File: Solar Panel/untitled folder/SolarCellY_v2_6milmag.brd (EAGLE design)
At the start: 100 x 82 mm, 23 parts

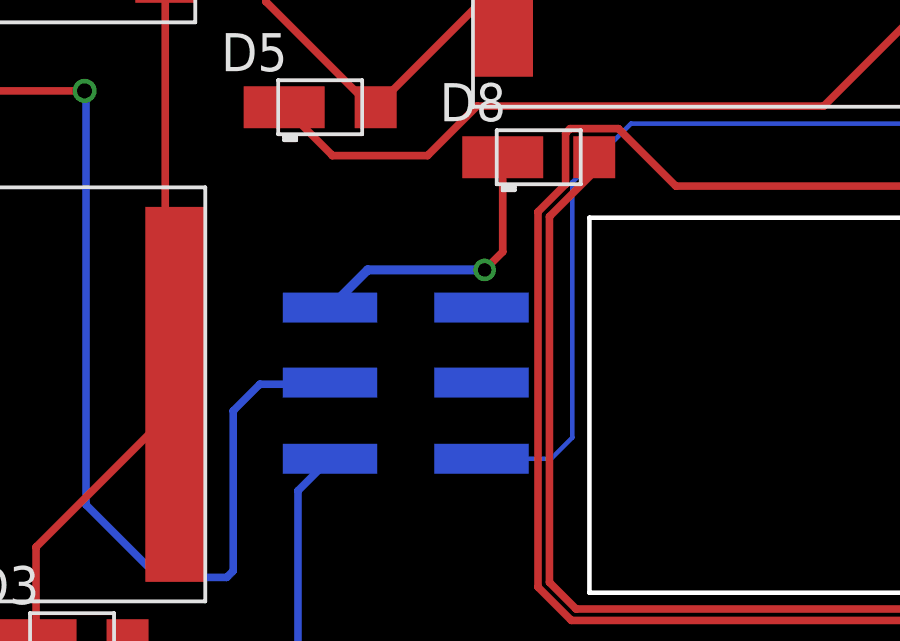
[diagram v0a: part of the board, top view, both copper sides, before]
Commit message: Finalized Y and created gerbers
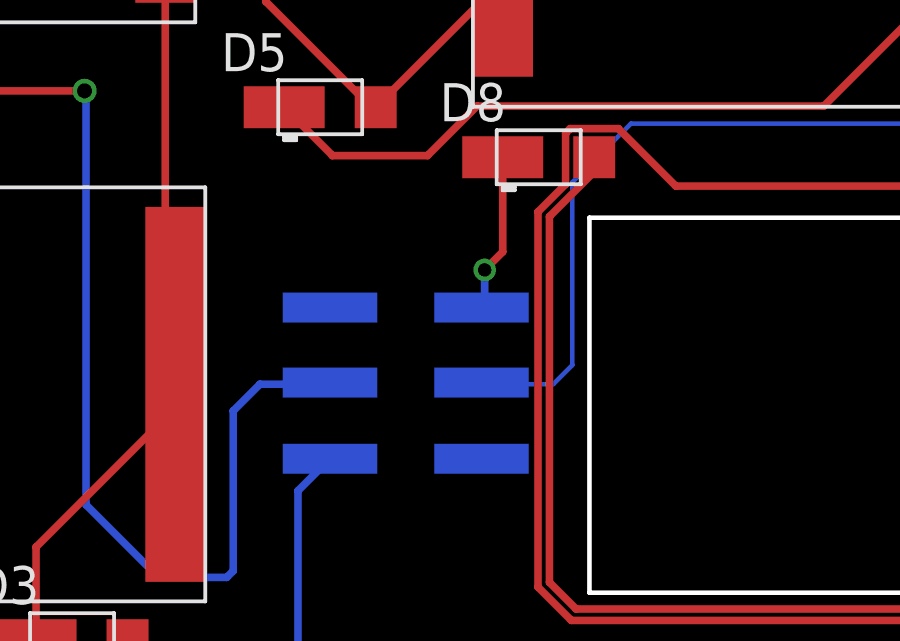
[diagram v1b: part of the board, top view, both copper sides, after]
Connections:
- net N$1: now also U$1.P$4; no longer U$1.P$2
- net N$14: now also U$1.P$6; no longer U$1.P$5
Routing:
- net N$14: track 9.68 -> 5.40 mm
- net N$1: track 54673.9 -> 54671.7 mm
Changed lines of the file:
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@@
 <layers>
 <layer number="1" name="Top" color="4" fill="1" visible="yes" active="yes"/>
-<layer number="2" name="Route2" color="16" fill="1" visible="yes" active="yes"/>
+<layer number="2" name="Route2" color="16" fill="1" visible="no" active="yes"/>
 <layer number="3" name="Route3" color="17" fill="1" visible="no" active="no"/>
 <layer number="4" name="Route4" color="18" fill="1" visible="no" active="no"/>
@@
 <wire x1="72.8472" y1="59.2836" x2="72.8472" y2="22.5552" width="0.1524" layer="15"/>
 <wire x1="72.8472" y1="22.5552" x2="27.7368" y2="22.5552" width="0.1524" layer="15"/>
+<contactref element="U$1" pad="P$4"/>
 <contactref element="U$1" pad="P$3"/>
 <wire x1="41.148" y1="50.546" x2="41.195115625" y2="50.546" width="0.254" layer="16"/>
@@
 <wire x1="41.148" y1="50.546" x2="9.906" y2="50.546" width="0.254" layer="1"/>
 <wire x1="9.906" y1="50.546" x2="8.636" y2="51.816" width="0.254" layer="1"/>
+<wire x1="72.5424" y1="48.895" x2="68.58" y2="48.895" width="0.1524" layer="2"/>
 <wire x1="8.636" y1="51.816" x2="2.413" y2="51.816" width="0.254" layer="1"/>
 <wire x1="2.413" y1="51.816" x2="2.286" y2="51.943" width="0.254" layer="1"/>
@@
 <wire x1="72.5424" y1="49.4538" x2="59.3598" y2="49.4538" width="0.1524" layer="16"/>
 <wire x1="59.3598" y1="49.4538" x2="57.404" y2="47.498" width="0.1524" layer="16"/>
-<wire x1="57.404" y1="47.498" x2="57.404" y2="38.989" width="0.1524" layer="16"/>
+<wire x1="56.769" y1="40.767" x2="54.356" y2="40.767" width="0.1524" layer="16"/>
+<wire x1="57.404" y1="47.498" x2="57.404" y2="41.402" width="0.1524" layer="16"/>
+<wire x1="57.404" y1="41.402" x2="56.769" y2="40.767" width="0.1524" layer="16"/>
 <wire x1="72.8472" y1="59.2836" x2="27.432" y2="59.2836" width="0.1524" layer="16"/>
+<wire x1="68.58" y1="48.895" x2="68.707" y2="48.768" width="0.1524" layer="2"/>
 <wire x1="68.707" y1="48.768" x2="68.707" y2="48.26" width="0.1524" layer="2"/>
+<wire x1="54.356" y1="40.767" x2="54.377" y2="40.822" width="0" layer="19" extent="16-16"/>
+<wire x1="27.432" y1="59.2836" x2="27.432" y2="59.2836" width="0" layer="19" extent="2-15"/>
+<wire x1="49.327" y1="40.822" x2="49.657" y2="40.767" width="0" layer="19" extent="16-16"/>
 <via x="68.707" y="48.26" extent="1-16" drill="0.45"/>
-<contactref element="U$1" pad="P$2"/>
-<wire x1="57.404" y1="38.989" x2="56.697" y2="38.282" width="0.1524" layer="16"/>
-<wire x1="56.697" y1="38.282" x2="54.377" y2="38.282" width="0.1524" layer="16"/>
-<wire x1="72.5424" y1="48.895" x2="68.834" y2="48.895" width="0.1524" layer="2"/>
-<wire x1="68.834" y1="48.895" x2="68.707" y2="48.768" width="0.1524" layer="2"/>
-<wire x1="49.657" y1="40.767" x2="49.327" y2="40.822" width="0" layer="19" extent="16-16"/>
-<wire x1="72.8472" y1="59.2836" x2="72.8472" y2="59.2836" width="0" layer="19" extent="2-15"/>
 </signal>
 <signal name="N$4">
@@
 <signal name="N$14">
 <contactref element="D8" pad="NEG"/>
+<contactref element="U$1" pad="P$6"/>
 <wire x1="55.085" y1="48.333" x2="55.085" y2="45.179" width="0.254" layer="1"/>
 <wire x1="55.085" y1="45.179" x2="54.483" y2="44.577" width="0.254" layer="1"/>
 <via x="54.483" y="44.577" extent="1-16" drill="0.45"/>
-<contactref element="U$1" pad="P$5"/>
-<wire x1="54.483" y1="44.577" x2="50.582" y2="44.577" width="0.3048" layer="16"/>
-<wire x1="50.582" y1="44.577" x2="49.327" y2="43.322" width="0.3048" layer="16"/>
+<wire x1="54.483" y1="44.577" x2="54.483" y2="43.18" width="0.254" layer="16"/>
+<wire x1="54.483" y1="43.18" x2="54.377" y2="43.322" width="0" layer="19" extent="16-16"/>
 </signal>
 <signal name="N$8">
